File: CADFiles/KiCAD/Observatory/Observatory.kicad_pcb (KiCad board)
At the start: 4 copper layers, 213.4 x 78.5 mm, 52 parts, among them J1 GND/CUT, J10 Dio_Jump, J11 nRF Connections, J12 Sulu Header, J13 Serial, J14 RsTx_Dio, J15 RsRx_Dio, J16 JScope Voltage, J17 WaveGen. 1 Mux Config., J18 JScope I+, J19 JScope I-, J2 Analog Discovery Connection, J20 Mounting Hole, J21 Mounting Hole, J22 Mounting Hole, J23 Mounting Hole, J24 prog. LED, J3 Digitial Discovery Connection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, J4 Scope 1 Mux Config., J5 Scope 2 Mux Config., J6 JScope V+, J7 JScope V-, J8 JScope Current IO, J9 5V_in, Q1 2N7002, SW1 SW_DIP_x08, SW2 SW_DIP_x08, U1 1, U2 Scope 1 Mux, U3 Wave Gen. Mux, U4 Scope 2 Mux, U5 Pico

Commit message: AD DC(-) error fixed. Jumpers added for feet grounds and DC supplies
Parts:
- added J25: Jumper, Connector_PinHeader_2.54mm:PinHeader_1x02_P2.54mm_Vertical, F.Cu at (161.4, 40.3)
- added J26: Jumper, Jumper:SolderJumper-2_P1.3mm_Open_Pad1.0x1.5mm, F.Cu at (50.8, 110.8)
- added J27: Jumper, Jumper:SolderJumper-2_P1.3mm_Open_Pad1.0x1.5mm, F.Cu at (50.6, 38.9)
- added J28: Jumper, Jumper:SolderJumper-2_P1.3mm_Open_Pad1.0x1.5mm, F.Cu at (244.8, 110.9)
- added J29: Jumper, Jumper:SolderJumper-2_P1.3mm_Open_Pad1.0x1.5mm, F.Cu at (244.8, 38.9)
- added J30: Jumper, Connector_PinHeader_2.54mm:PinHeader_1x02_P2.54mm_Vertical, F.Cu at (62.2, 102.7)
- J9: value 5V_in -> EXT_BAT
- moved J21 1.30 mm to (45.4, 38.9)
- moved J23 1.30 mm to (250.2, 38.9)
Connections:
- J1 pad 1: AD_DC_Supply- -> AD_Scope1-
- J11 pad 1: AD_DC_Supply- -> AD_Scope1-
- J12 pad 1: AD_DC_Supply- -> AD_Scope1-
- J12 pad 11: AD_DC_Supply- -> AD_Scope1-
- J12 pad 12: AD_DC_Supply+ -> Net-(J12-Pin_12)
- J12 pad 2: AD_DC_Supply- -> AD_Scope1-
- J12 pad 3: AD_DC_Supply- -> AD_Scope1-
- J16 pad 5: AD_DC_Supply+ -> Net-(J12-Pin_12)
- J17 pad 1: AD_DC_Supply- -> AD_Scope1-
- J17 pad 2: AD_DC_Supply- -> AD_Scope1-
- J17 pad 3: AD_DC_Supply- -> AD_Scope1-
- J17 pad 4: AD_DC_Supply- -> AD_Scope1-
- J17 pad 5: AD_DC_Supply- -> AD_Scope1-
- J2 pad 11: AD_DC_Supply- -> AD_Scope1-
- J2 pad 12: AD_DC_Supply- -> AD_Scope1-
- J2 pad 2: AD_DC_Supply- -> AD_Scope1-
- J2 pad 4: AD_DC_Supply- -> AD_Scope1-
- J2 pad 5: AD_DC_Supply- -> AD_Scope1-
- J2 pad 6: AD_DC_Supply- -> AD_Scope1-
- J2 pad 7: AD_DC_Supply+ -> Net-(J2-Pin_7)
- J20 pad 1: unconnected-(J20-Pin_1-Pad1)_7 -> Net-(J20-Pin_1)
- J21 pad 1: unconnected-(J21-Pin_1-Pad1)_8 -> Net-(J21-Pin_1)
- J22 pad 1: unconnected-(J22-Pin_1-Pad1) -> Net-(J22-Pin_1)
- J23 pad 1: unconnected-(J23-Pin_1-Pad1)_4 -> Net-(J23-Pin_1)
- J3 pad 1: AD_DC_Supply- -> AD_Scope1-
- J3 pad 11: AD_DC_Supply- -> AD_Scope1-
- J3 pad 12: AD_DC_Supply- -> AD_Scope1-
- J3 pad 2: AD_DC_Supply- -> AD_Scope1-
- J3 pad 21: AD_DC_Supply- -> AD_Scope1-
- J3 pad 22: AD_DC_Supply- -> AD_Scope1-
- J3 pad 31: AD_DC_Supply- -> AD_Scope1-
- J3 pad 32: AD_DC_Supply- -> AD_Scope1-
- J4 pad 1: AD_DC_Supply- -> AD_Scope1-
- J4 pad 2: AD_DC_Supply- -> AD_Scope1-
- J4 pad 3: AD_DC_Supply- -> AD_Scope1-
- J4 pad 4: AD_DC_Supply- -> AD_Scope1-
- J4 pad 5: AD_DC_Supply- -> AD_Scope1-
- J5 pad 1: AD_DC_Supply- -> AD_Scope1-
- J5 pad 2: AD_DC_Supply- -> AD_Scope1-
- J5 pad 3: AD_DC_Supply- -> AD_Scope1-
- J5 pad 4: AD_DC_Supply- -> AD_Scope1-
- J5 pad 5: AD_DC_Supply- -> AD_Scope1-
- J7 pad 2: AD_DC_Supply- -> AD_Scope1-
- J9 pad 1: AD_DC_Supply- -> AD_Scope1-
- J9 pad 2: AD_DC_Supply+ -> Net-(J12-Pin_12)
- R10 pad 1: AD_DC_Supply+ -> +5V
- R11 pad 1: AD_DC_Supply+ -> +5V
- R12 pad 1: AD_DC_Supply+ -> +5V
- R13 pad 1: AD_DC_Supply+ -> +5V
- R14 pad 1: AD_DC_Supply+ -> +5V
- R15 pad 1: AD_DC_Supply+ -> +5V
- R16 pad 1: AD_DC_Supply+ -> +5V
- R2 pad 1: AD_DC_Supply+ -> +5V
- R3 pad 1: AD_DC_Supply+ -> +5V
- R4 pad 1: AD_DC_Supply+ -> +5V
- R5 pad 1: AD_DC_Supply+ -> +5V
- R6 pad 1: AD_DC_Supply+ -> +5V
- R7 pad 1: AD_DC_Supply+ -> +5V
- R8 pad 1: AD_DC_Supply+ -> +5V
- R9 pad 1: AD_DC_Supply+ -> +5V
- U1 pad 10b: AD_DC_Supply- -> AD_Scope1-
- U1 pad 11c: AD_DC_Supply- -> AD_Scope1-
- U1 pad 12c: AD_DC_Supply+ -> Net-(J12-Pin_12)
- U1 pad 19a: AD_DC_Supply- -> AD_Scope1-
- U1 pad 1a: AD_DC_Supply- -> AD_Scope1-
- U1 pad 1c: AD_DC_Supply- -> AD_Scope1-
- U1 pad 20a: AD_DC_Supply- -> AD_Scope1-
- U1 pad 2c: AD_DC_Supply- -> AD_Scope1-
- U1 pad 3b: AD_DC_Supply- -> AD_Scope1-
- U1 pad 3c: AD_DC_Supply- -> AD_Scope1-
- U2 pad 13: AD_DC_Supply+ -> +5V
- U2 pad 14: AD_DC_Supply+ -> +5V
- U2 pad 20: AD_DC_Supply- -> AD_Scope1-
- U2 pad 21: AD_DC_Supply- -> AD_Scope1-
- U2 pad 22: AD_DC_Supply- -> AD_Scope1-
- U2 pad 23: AD_DC_Supply- -> AD_Scope1-
- U2 pad 24: AD_DC_Supply- -> AD_Scope1-
- U3 pad 13: AD_DC_Supply+ -> +5V
- U3 pad 14: AD_DC_Supply+ -> +5V
- U3 pad 20: AD_DC_Supply- -> AD_Scope1-
- U3 pad 21: AD_DC_Supply- -> AD_Scope1-
- U3 pad 22: AD_DC_Supply- -> AD_Scope1-
- U3 pad 23: AD_DC_Supply- -> AD_Scope1-
- U3 pad 24: AD_DC_Supply- -> AD_Scope1-
- U4 pad 13: AD_DC_Supply+ -> +5V
- U4 pad 14: AD_DC_Supply+ -> +5V
- U4 pad 20: AD_DC_Supply- -> AD_Scope1-
- U4 pad 21: AD_DC_Supply- -> AD_Scope1-
- U4 pad 22: AD_DC_Supply- -> AD_Scope1-
- U4 pad 23: AD_DC_Supply- -> AD_Scope1-
- U4 pad 24: AD_DC_Supply- -> AD_Scope1-
- U5 pad 13: AD_DC_Supply- -> AD_Scope1-
- U5 pad 18: AD_DC_Supply- -> AD_Scope1-
- U5 pad 23: AD_DC_Supply- -> AD_Scope1-
- U5 pad 28: AD_DC_Supply- -> AD_Scope1-
- U5 pad 3: AD_DC_Supply- -> AD_Scope1-
- U5 pad 33: AD_DC_Supply- -> AD_Scope1-
- U5 pad 38: AD_DC_Supply- -> AD_Scope1-
- U5 pad 39: AD_DC_Supply+ -> +5V
- U5 pad 8: AD_DC_Supply- -> AD_Scope1-
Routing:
- net AD_DC_Supply-: track 95.6 -> 0.00 mm, vias 234 -> 0
- net Net-(J12-Pin_12): track 0.00 -> 93.0 mm
- net Net-(J2-Pin_7): track 0.00 -> 89.2 mm
- net AD_Scope1-: track 0.00 -> 86.0 mm, vias 0 -> 238
- net AD_DC_Supply+: track 49.8 -> 0.00 mm, vias 19 -> 0
- net +5V: track 0.00 -> 42.3 mm, vias 0 -> 21
- net Net-(J22-Pin_1): track 0.00 -> 4.77 mm
- net Net-(J20-Pin_1): track 0.00 -> 4.75 mm
- net Net-(J23-Pin_1): track 0.00 -> 4.70 mm
- net Net-(J21-Pin_1): track 0.00 -> 4.60 mm
- added copper zone on In2.Cu, net +5V
- added copper zone on B.Cu, net AD_Scope1-
- added copper zone on In1.Cu, net AD_Scope1-
- removed copper zone on In2.Cu, net AD_DC_Supply+
- removed copper zone on B.Cu, net AD_DC_Supply-
- removed copper zone on In1.Cu, net AD_DC_Supply-
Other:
- board size 213.4 x 78.5 mm -> 213.4 x 79.7 mm
- board text added: "AD_DC+ supply to observatory"
- board text added: "EXT_BAT to observatory"

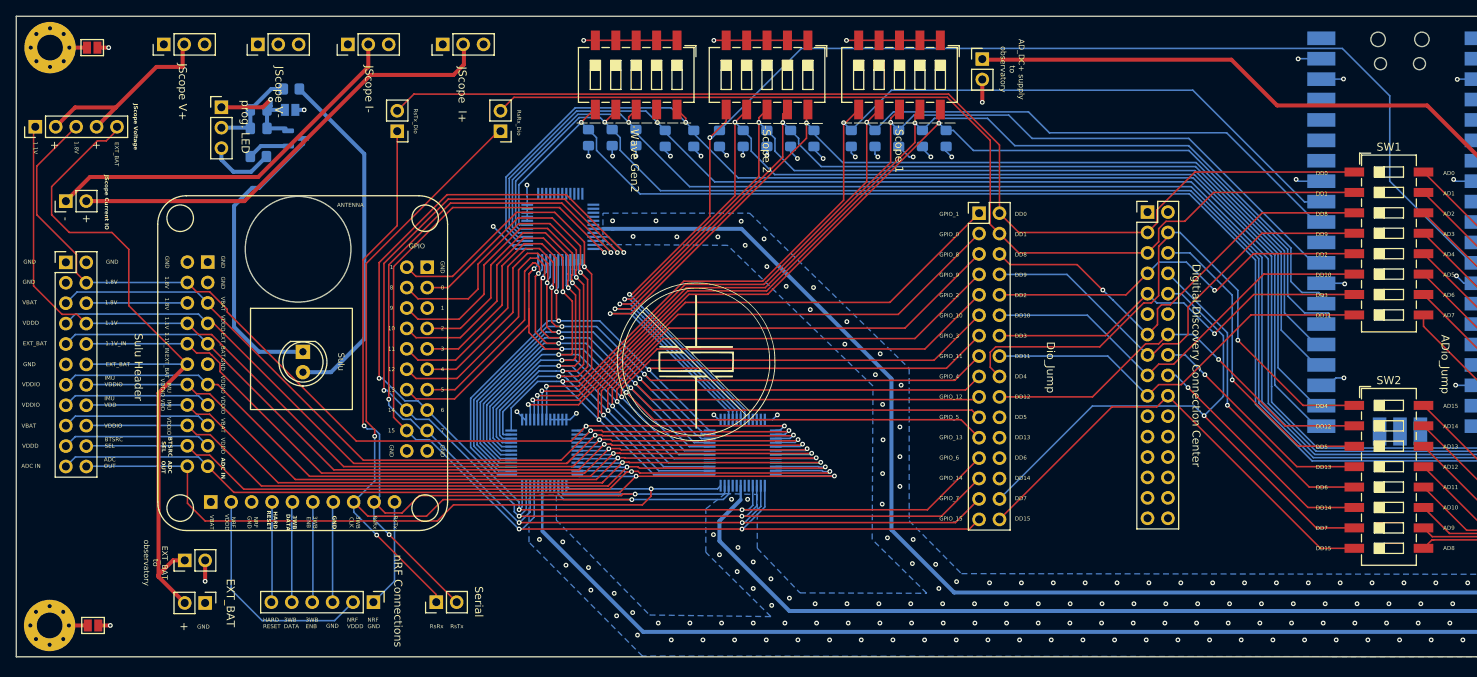
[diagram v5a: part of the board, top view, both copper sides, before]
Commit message: Fixs: Disconnnect pico Vsys from board. RX/TX pin errors, 3WD_CLK pin.
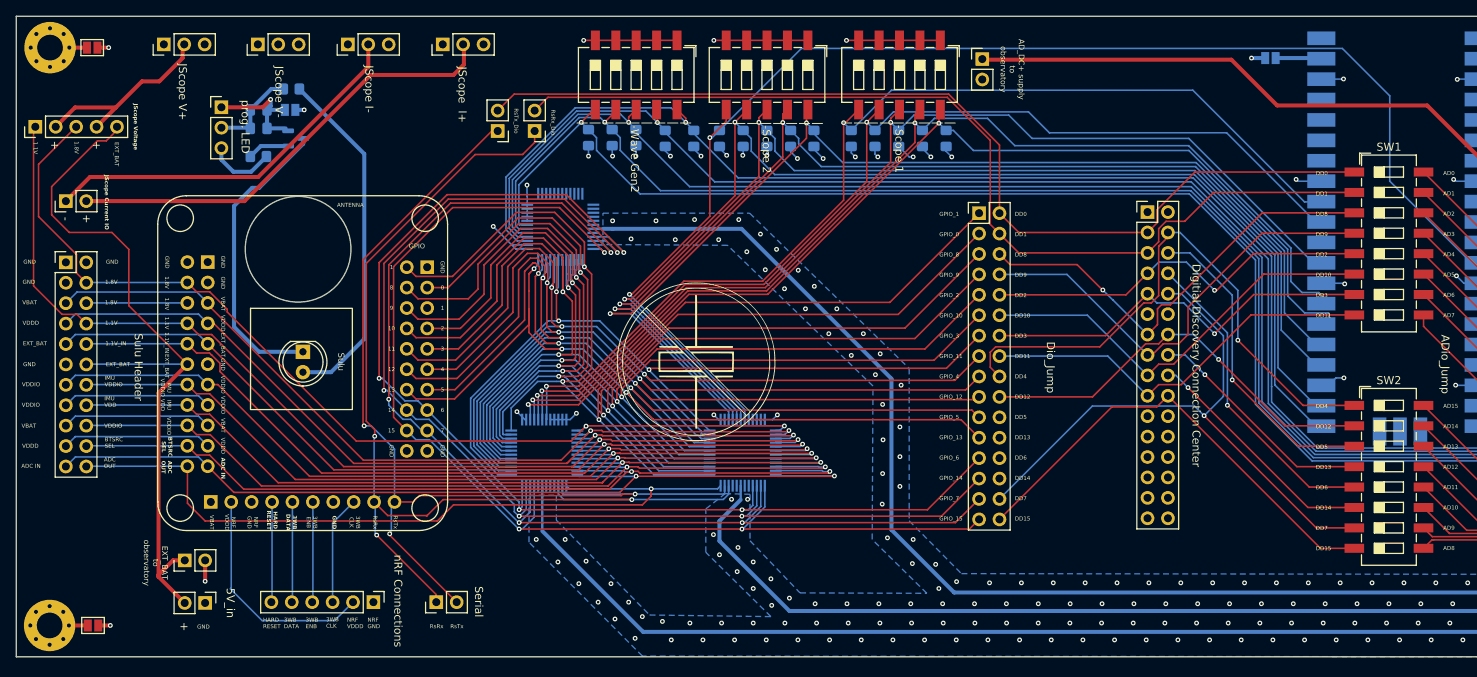
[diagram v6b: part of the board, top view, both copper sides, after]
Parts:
- added J31: Jumper, Jumper:SolderJumper-2_P1.3mm_Open_Pad1.0x1.5mm, B.Cu at (197.2, 40.2)
- J9: value EXT_BAT -> 5V_in
- moved J14 12.5 mm to (101.1, 49.3)
- moved J15 4.25 mm to (105.7, 49.3)
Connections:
- U1 pad 10b: AD_Scope1- -> Scope 1 Mux  30
- U1 pad 7b: Net-(J11-Pin_3) -> AD_Scope1-
- U1 pad 8b: Scope 1 Mux  31 -> Net-(J11-Pin_3)
- U1 pad 9b: Scope 1 Mux  30 -> Scope 1 Mux  31
- U5 pad 39: +5V -> Net-(J31-Pin_2)
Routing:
- net AD_Scope1-: track 86.0 -> 72.5 mm, vias 238 -> 245
- net DD_DIN_0: track 136.1 -> 123.6 mm
- net Net-(J31-Pin_2): track 0.00 -> 6.65 mm
- net +5V: track 42.3 -> 37.9 mm, vias 21 -> 20
- net DD_DIN_1: track 125.2 -> 120.9 mm
- net Scope 1 Mux  30: track 122.5 -> 124.5 mm
- net Net-(J11-Pin_3): track 12.5 -> 13.8 mm
- net Scope 1 Mux  31: track 131.5 -> 132.7 mm
- net JS_V+: track 25.2 -> 24.5 mm
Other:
- board text added: "3WB CLK"
- board text added: "V_sys to observatory supply"
